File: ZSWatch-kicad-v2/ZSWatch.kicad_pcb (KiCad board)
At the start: 4 copper layers, 41 x 38 mm, 81 parts, among them IC1 ESDALC6V1W5, IC2 XC9265C181MR-G, IC3 TPS61023DRLT, IC4 MAX30101EFD+T, IC5 FAN5622SX, IC6 BMI270, IC7 LIS2MDLTR, IC8 AT25SF128A-MHB-T, J2 Charger and programming heade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, M1 Vibrator DC Motor, U1 MAX1811ESA+, U10 0_NORA-B106, U11 NTS0104GU12, U13 GC9A01A_CST816S, U2 DMC2400UV-7, U3 NCV300LSN36T1G, U4 BMP581, U5 BME688, U6 DRV2603RUNT, U7 XC9265A331MR-G

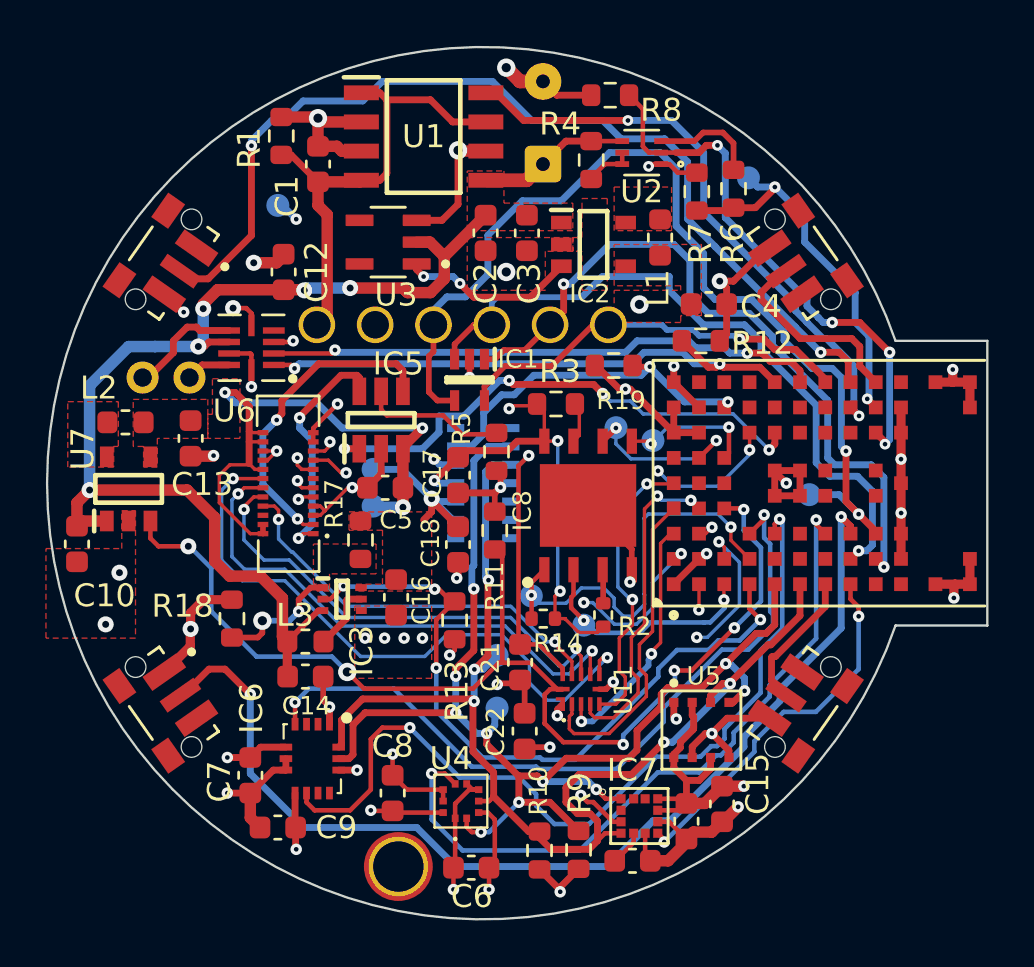
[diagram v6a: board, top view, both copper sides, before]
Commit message: PCB: Tidy up some traces and vias for external flash feature.
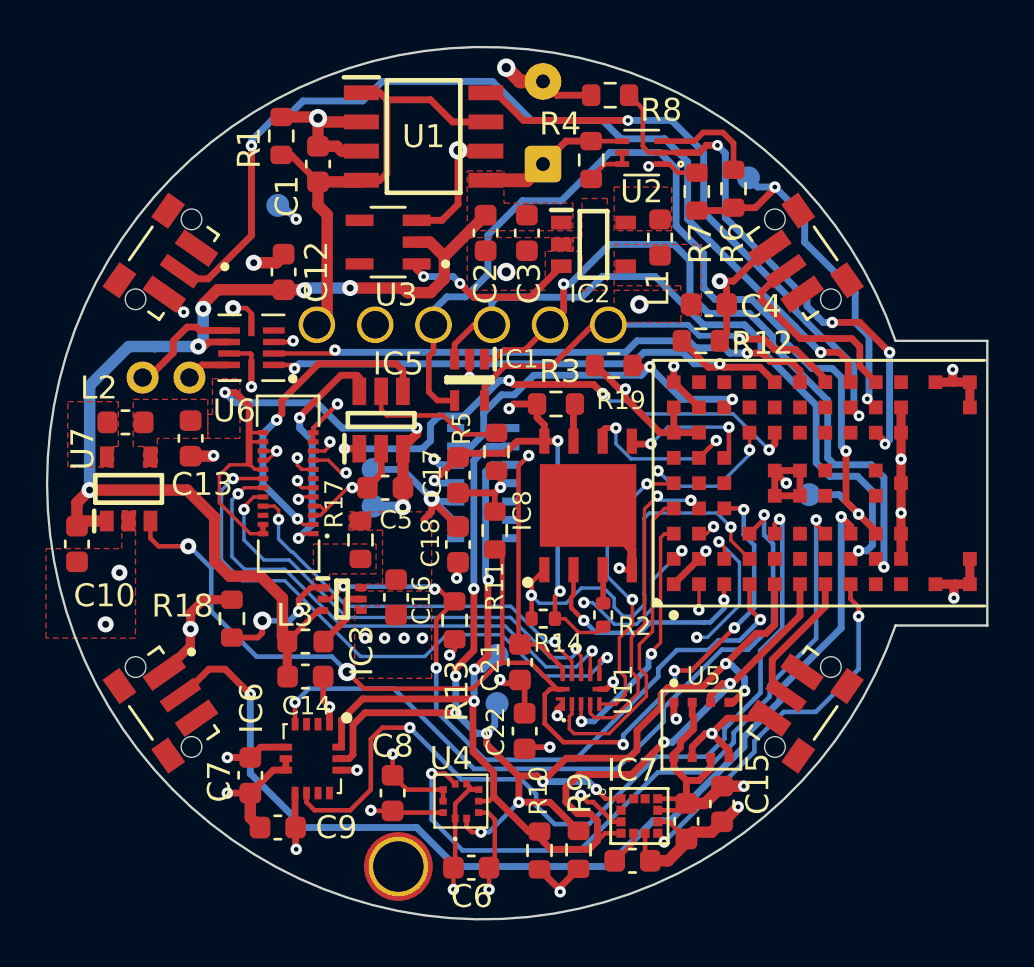
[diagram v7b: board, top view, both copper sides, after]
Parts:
- removed CLK, CS, SI, SO: MR, TestPoint:TestPoint_Pad_D1.0mm
- moved G*** 7.57 mm to (97.4, 105.2)
- moved TP9 0.20 mm to (98.5, 110.0)
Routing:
- net /TOUCH_HIGH_RST-SDA: track 27.2 -> 25.8 mm
